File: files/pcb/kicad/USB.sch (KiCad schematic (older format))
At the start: 7 parts, among them CON1 USB_MINI_B

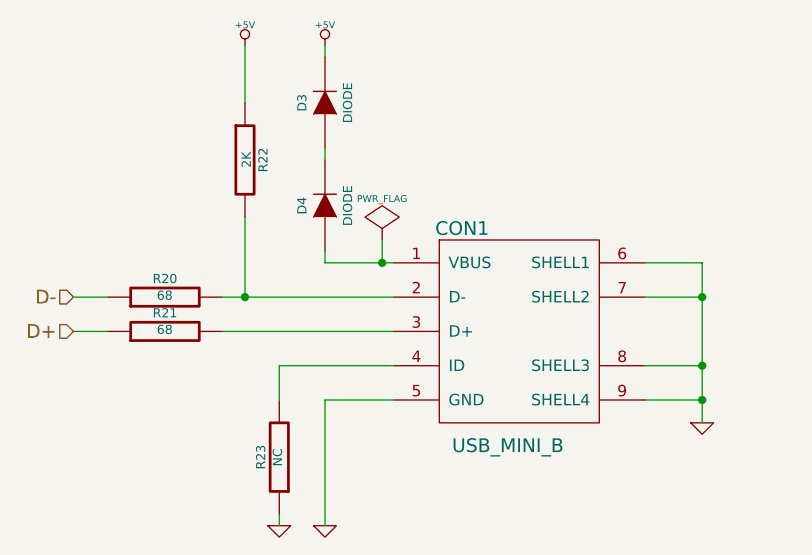
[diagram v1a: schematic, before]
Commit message: 設計見直し
部品見直し
USB・DCジャック自動切り替え
マイコンを下段のボードに移動
ニキシー管駆動電源を上段ボードに移動
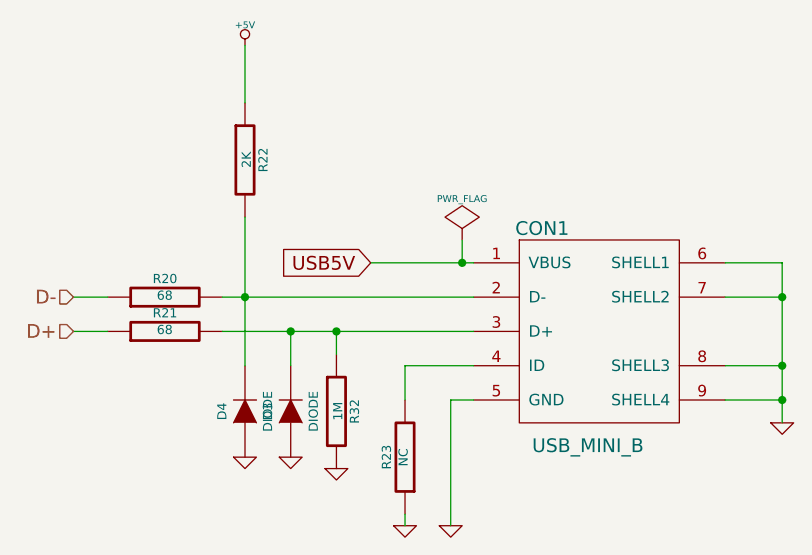
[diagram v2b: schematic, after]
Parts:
- added R32: 1M, ~, symbol R
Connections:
- net +5V: no longer D3.2 (K)
- net GND: now also D3.1 (A), D4.1 (A), R32.2
- net at CON1.2 (D-), R20.2, R22.2: now also D4.2 (K)
- net at CON1.3 (D+), R21.2: now also D3.2 (K), R32.1
- net USB5V: now reaches CON1.1 (VBUS)
- net USB5V: no longer D4.1 (A)
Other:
- moved on the sheet: CON1, D3, D4, R23
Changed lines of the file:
@@
 $Descr A4 11693 8268
 encoding utf-8
-Sheet 6 11
+Sheet 6 8
 Title ""
-Date "31 aug 2014"
+Date "1 sep 2014"
 Rev ""
 Comp ""
@@
 $EndComp
 $Comp
-L +5V #PWR030
-U 1 1 53F90F9E
-P 5300 2950
-F 0 "#PWR030" H 5300 3040 20  0001 C CNN
-F 1 "+5V" H 5300 3040 30  0000 C CNN
-F 2 "" H 5300 2950 60  0000 C CNN
-F 3 "" H 5300 2950 60  0000 C CNN
-	1    5300 2950
-	1    0    0    -1
-$EndComp
-$Comp
 L R R23
 U 1 1 53F90FB6
-P 5100 4750
-F 0 "R23" V 5180 4750 40  0000 C CNN
-F 1 "NC" V 5107 4751 40  0000 C CNN
-F 2 "~" V 5030 4750 30  0000 C CNN
-F 3 "~" H 5100 4750 30  0000 C CNN
-	1    5100 4750
+P 5650 4750
+F 0 "R23" V 5730 4750 40  0000 C CNN
+F 1 "NC" V 5657 4751 40  0000 C CNN
+F 2 "~" V 5580 4750 30  0000 C CNN
+F 3 "~" H 5650 4750 30  0000 C CNN
+	1    5650 4750
 	-1   0    0    1
 $EndComp
@@
 $EndComp
 $Comp
-L +5V #PWR031
+L +5V #PWR036
 U 1 1 53F91040
 P 4950 2950
-F 0 "#PWR031" H 4950 3040 20  0001 C CNN
+F 0 "#PWR036" H 4950 3040 20  0001 C CNN
 F 1 "+5V" H 4950 3040 30  0000 C CNN
 F 2 "" H 4950 2950 60  0000 C CNN
@@
 $EndComp
 $Comp
-L GND #PWR032
+L GND #PWR037
 U 1 1 53F910A2
-P 5100 5050
-F 0 "#PWR032" H 5100 5050 30  0001 C CNN
-F 1 "GND" H 5100 4980 30  0001 C CNN
-F 2 "" H 5100 5050 60  0000 C CNN
-F 3 "" H 5100 5050 60  0000 C CNN
-	1    5100 5050
-	1    0    0    -1
-$EndComp
-$Comp
-L GND #PWR033
+P 5650 5050
+F 0 "#PWR037" H 5650 5050 30  0001 C CNN
+F 1 "GND" H 5650 4980 30  0001 C CNN
+F 2 "" H 5650 5050 60  0000 C CNN
+F 3 "" H 5650 5050 60  0000 C CNN
+	1    5650 5050
+	1    0    0    -1
+$EndComp
+$Comp
+L GND #PWR038
 U 1 1 53F910B1
-P 5300 5050
-F 0 "#PWR033" H 5300 5050 30  0001 C CNN
-F 1 "GND" H 5300 4980 30  0001 C CNN
-F 2 "" H 5300 5050 60  0000 C CNN
-F 3 "" H 5300 5050 60  0000 C CNN
-	1    5300 5050
+P 5850 5050
+F 0 "#PWR038" H 5850 5050 30  0001 C CNN
+F 1 "GND" H 5850 4980 30  0001 C CNN
+F 2 "" H 5850 5050 60  0000 C CNN
+F 3 "" H 5850 5050 60  0000 C CNN
+	1    5850 5050
 	1    0    0    -1
 $EndComp
@@
 L DIODE D4
 U 1 1 53F910F0
-P 5300 3650
-F 0 "D4" H 5300 3750 40  0000 C CNN
-F 1 "DIODE" H 5300 3550 40  0000 C CNN
-F 2 "~" H 5300 3650 60  0000 C CNN
-F 3 "~" H 5300 3650 60  0000 C CNN
-	1    5300 3650
+P 4950 4550
+F 0 "D4" H 4950 4650 40  0000 C CNN
+F 1 "DIODE" H 4950 4450 40  0000 C CNN
+F 2 "~" H 4950 4550 60  0000 C CNN
+F 3 "~" H 4950 4550 60  0000 C CNN
+	1    4950 4550
 	0    -1   -1   0
 $EndComp
@@
 L DIODE D3
 U 1 1 53F91104
-P 5300 3200
-F 0 "D3" H 5300 3300 40  0000 C CNN
-F 1 "DIODE" H 5300 3100 40  0000 C CNN
-F 2 "~" H 5300 3200 60  0000 C CNN
-F 3 "~" H 5300 3200 60  0000 C CNN
-	1    5300 3200
-	0    -1   -1   0
-$EndComp
-$Comp
-L PWR_FLAG #FLG034
+P 5150 4550
+F 0 "D3" H 5150 4650 40  0000 C CNN
+F 1 "DIODE" H 5150 4450 40  0000 C CNN
+F 2 "~" H 5150 4550 60  0000 C CNN
+F 3 "~" H 5150 4550 60  0000 C CNN
+	1    5150 4550
+	0    -1   -1   0
+$EndComp
+$Comp
+L PWR_FLAG #FLG039
 U 1 1 53FCAA4C
-P 5550 3800
-F 0 "#FLG034" H 5550 3895 30  0001 C CNN
-F 1 "PWR_FLAG" H 5550 3980 30  0000 C CNN
-F 2 "" H 5550 3800 60  0000 C CNN
-F 3 "" H 5550 3800 60  0000 C CNN
-	1    5550 3800
-	1    0    0    -1
-$EndComp
-$Comp
-L GND #PWR035
+P 5900 3800
+F 0 "#FLG039" H 5900 3895 30  0001 C CNN
+F 1 "PWR_FLAG" H 5900 3980 30  0000 C CNN
+F 2 "" H 5900 3800 60  0000 C CNN
+F 3 "" H 5900 3800 60  0000 C CNN
+	1    5900 3800
+	1    0    0    -1
+$EndComp
+$Comp
+L GND #PWR040
 U 1 1 53FCBB40
-P 6950 4600
-F 0 "#PWR035" H 6950 4600 30  0001 C CNN
-F 1 "GND" H 6950 4530 30  0001 C CNN
-F 2 "" H 6950 4600 60  0000 C CNN
-F 3 "" H 6950 4600 60  0000 C CNN
-	1    6950 4600
-	1    0    0    -1
-$EndComp
-Wire Wire Line
-	4850 4050 5600 4050
-Wire Wire Line
-	4850 4200 5600 4200
+P 7300 4600
+F 0 "#PWR040" H 7300 4600 30  0001 C CNN
+F 1 "GND" H 7300 4530 30  0001 C CNN
+F 2 "" H 7300 4600 60  0000 C CNN
+F 3 "" H 7300 4600 60  0000 C CNN
+	1    7300 4600
+	1    0    0    -1
+$EndComp
+Wire Wire Line
+	4850 4050 5950 4050
+Wire Wire Line
+	4850 4200 5950 4200
 Wire Wire Line
 	4200 4050 4350 4050
@@
 	4350 4200 4200 4200
 Wire Wire Line
-	4950 3700 4950 4050
+	4950 3700 4950 4350
 Connection ~ 4950 4050
 Wire Wire Line
 	4950 3200 4950 2950
 Wire Wire Line
-	5600 4500 5300 4500
-Wire Wire Line
-	5300 4500 5300 5050
-Wire Wire Line
-	5600 4350 5100 4350
-Wire Wire Line
-	5100 4350 5100 4500
-Wire Wire Line
-	5100 5000 5100 5050
-Wire Wire Line
-	5300 3450 5300 3400
-Wire Wire Line
-	5300 3900 5300 3850
-Wire Wire Line
-	5300 3000 5300 2950
-Wire Wire Line
-	5600 3900 5300 3900
-Wire Wire Line
-	5550 3800 5550 3900
-Connection ~ 5550 3900
-Wire Wire Line
-	6700 3900 6950 3900
-Wire Wire Line
-	6950 3900 6950 4600
-Wire Wire Line
-	6700 4050 6950 4050
-Connection ~ 6950 4050
-Wire Wire Line
-	6700 4350 6950 4350
-Connection ~ 6950 4350
-Wire Wire Line
-	6700 4500 6950 4500
-Connection ~ 6950 4500
+	5950 4500 5850 4500
+Wire Wire Line
+	5850 4500 5850 5050
+Wire Wire Line
+	5950 4350 5650 4350
+Wire Wire Line
+	5650 4350 5650 4500
+Wire Wire Line
+	5650 5000 5650 5050
+Wire Wire Line
+	5150 4350 5150 4200
+Wire Wire Line
+	5500 3900 5950 3900
+Wire Wire Line
+	5900 3800 5900 3900
+Connection ~ 5900 3900
+Wire Wire Line
+	7050 3900 7300 3900
+Wire Wire Line
+	7300 3900 7300 4600
+Wire Wire Line
+	7050 4050 7300 4050
+Connection ~ 7300 4050
+Wire Wire Line
+	7050 4350 7300 4350
+Connection ~ 7300 4350
+Wire Wire Line
+	7050 4500 7300 4500
+Connection ~ 7300 4500
 $Comp
 L USB_MINI_B CON1
 U 1 1 53FCC671
-P 6150 4200
-F 0 "CON1" H 5900 4650 60  0000 C CNN
-F 1 "USB_MINI_B" H 6100 3700 60  0000 C CNN
-F 2 "~" H 6150 4200 60  0000 C CNN
-F 3 "~" H 6150 4200 60  0000 C CNN
-	1    6150 4200
-	1    0    0    -1
-$EndComp
+P 6500 4200
+F 0 "CON1" H 6250 4650 60  0000 C CNN
+F 1 "USB_MINI_B" H 6450 3700 60  0000 C CNN
+F 2 "~" H 6500 4200 60  0000 C CNN
+F 3 "~" H 6500 4200 60  0000 C CNN
+	1    6500 4200
+	1    0    0    -1
+$EndComp
+$Comp
+L R R32
+U 1 1 5404B94E
+P 5350 4550
+F 0 "R32" V 5430 4550 40  0000 C CNN
+F 1 "1M" V 5357 4551 40  0000 C CNN
+F 2 "~" V 5280 4550 30  0000 C CNN
+F 3 "~" H 5350 4550 30  0000 C CNN
+	1    5350 4550
+	1    0    0    -1
+$EndComp
+Connection ~ 5150 4200
+Wire Wire Line
+	5350 4300 5350 4200
+Connection ~ 5350 4200
+$Comp
+L GND #PWR041
+U 1 1 5404B98B
+P 5350 4800
+F 0 "#PWR041" H 5350 4800 30  0001 C CNN
+F 1 "GND" H 5350 4730 30  0001 C CNN
+F 2 "" H 5350 4800 60  0000 C CNN
+F 3 "" H 5350 4800 60  0000 C CNN
+	1    5350 4800
+	1    0    0    -1
+$EndComp
+$Comp
+L GND #PWR042
+U 1 1 5404B998
+P 5150 4750
+F 0 "#PWR042" H 5150 4750 30  0001 C CNN
+F 1 "GND" H 5150 4680 30  0001 C CNN
+F 2 "" H 5150 4750 60  0000 C CNN
+F 3 "" H 5150 4750 60  0000 C CNN
+	1    5150 4750
+	1    0    0    -1
+$EndComp
+$Comp
+L GND #PWR043
+U 1 1 5404B99E
+P 4950 4750
+F 0 "#PWR043" H 4950 4750 30  0001 C CNN
+F 1 "GND" H 4950 4680 30  0001 C CNN
+F 2 "" H 4950 4750 60  0000 C CNN
+F 3 "" H 4950 4750 60  0000 C CNN
+	1    4950 4750
+	1    0    0    -1
+$EndComp
+Text GLabel 5500 3900 0    60   Input ~ 0
+USB5V
 $EndSCHEMATC
